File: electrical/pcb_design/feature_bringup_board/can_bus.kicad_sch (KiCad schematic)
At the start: 9 parts, among them J7 Molex_504050-0691, J8 Molex_504050-0691, U4 TCAN330DR

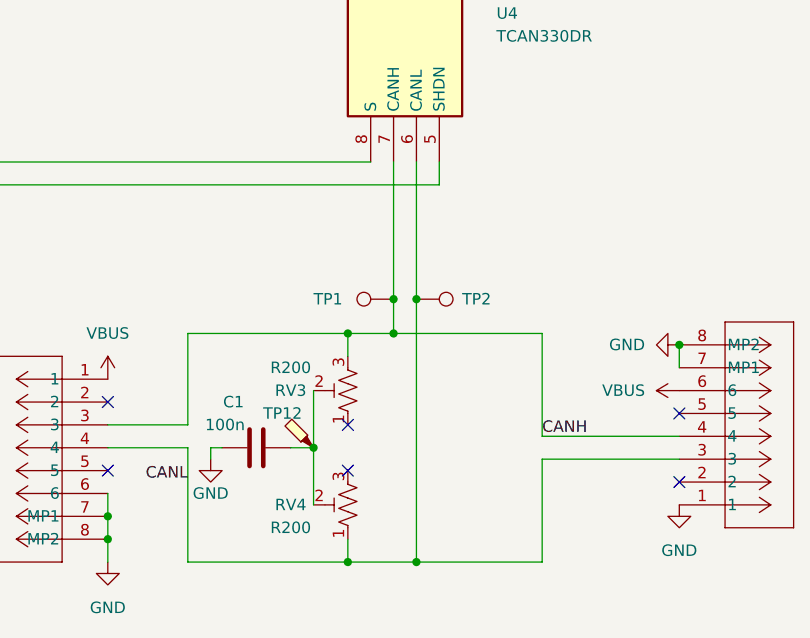
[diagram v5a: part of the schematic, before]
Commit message: Added 3rd button header. Also, fixed bugs introduced by cosmetic schematic changes.
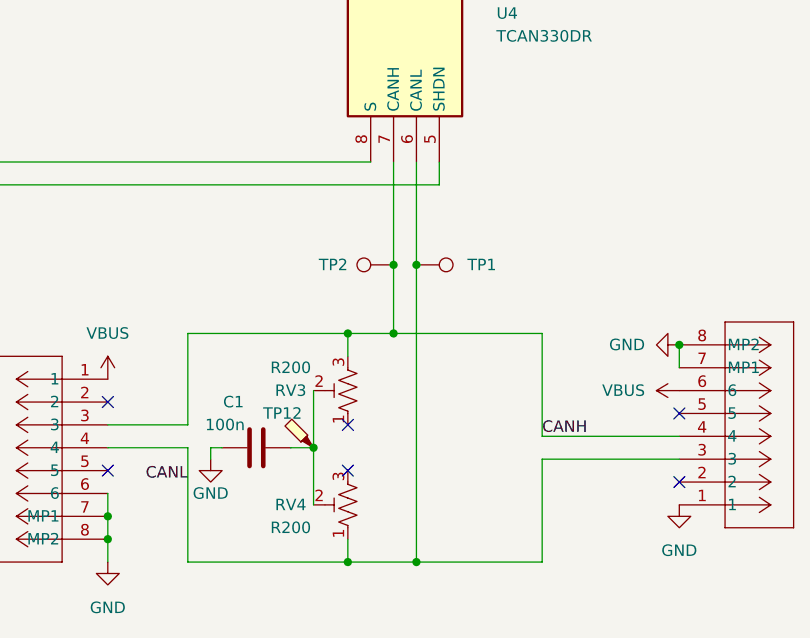
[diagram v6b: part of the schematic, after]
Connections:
- net CANH: now also TP2.1; no longer TP1.1
- net CANL: now also TP1.1; no longer TP2.1
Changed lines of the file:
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@@
   (junction (at 132.08 132.08) (diameter 0) (color 0 0 0 0)
   )
+  (junction (at 163.83 104.14) (diameter 0) (color 0 0 0 0)
+  )
   (junction (at 154.94 124.46) (diameter 0) (color 0 0 0 0)
   )
@@
   (junction (at 132.08 134.62) (diameter 0) (color 0 0 0 0)
   )
-  (junction (at 166.37 107.95) (diameter 0) (color 0 0 0 0)
-  )
-  (junction (at 163.83 107.95) (diameter 0) (color 0 0 0 0)
-  )
   (junction (at 166.37 137.16) (diameter 0) (color 0 0 0 0)
   )
   (junction (at 163.83 111.76) (diameter 0) (color 0 0 0 0)
+  )
+  (junction (at 166.37 104.14) (diameter 0) (color 0 0 0 0)
   )
   (no_connect (at 195.58 120.65))
@@
     (stroke (width 0) (type default))
   )
-  (wire (pts (xy 166.37 107.95) (xy 166.37 137.16))
+  (wire (pts (xy 166.37 92.71) (xy 166.37 104.14))
     (stroke (width 0) (type default))
   )
@@
     (stroke (width 0) (type default))
   )
-  (wire (pts (xy 166.37 92.71) (xy 166.37 107.95))
-    (stroke (width 0) (type default))
-  )
   (wire (pts (xy 180.34 123.19) (xy 180.34 111.76))
     (stroke (width 0) (type default))
@@
     (stroke (width 0) (type default))
   )
+  (wire (pts (xy 166.37 104.14) (xy 166.37 137.16))
+    (stroke (width 0) (type default))
+  )
   (wire (pts (xy 132.08 134.62) (xy 132.08 137.16))
     (stroke (width 0) (type default))
@@
     (stroke (width 0) (type default))
   )
+  (wire (pts (xy 163.83 104.14) (xy 163.83 111.76))
+    (stroke (width 0) (type default))
+  )
   (wire (pts (xy 158.75 137.16) (xy 166.37 137.16))
     (stroke (width 0) (type default))
@@
     (stroke (width 0) (type default))
   )
-  (wire (pts (xy 163.83 92.71) (xy 163.83 107.95))
-    (stroke (width 0) (type default))
-  )
-  (wire (pts (xy 163.83 107.95) (xy 163.83 111.76))
+  (wire (pts (xy 163.83 92.71) (xy 163.83 104.14))
     (stroke (width 0) (type default))
   )
@@
     )
   )
-  (symbol (lib_id "TVSC:TestPoint_Keystone_5002") (at 166.37 107.95 270) (unit 1)
-    (in_bom yes) (on_board yes) (dnp no)
-    (property "Reference" "TP2" (at 171.45 107.95 90)
-      (effects (font (size 1.27 1.27)) (justify left))
-    )
-    (property "Value" "TestPoint" (at 168.402 110.49 0)
-      (effects (font (size 1.27 1.27)) (justify left) hide)
-    )
-    (property "Footprint" "footprints:Keystone_5001" (at 166.37 113.03 0)
-      (effects (font (size 1.27 1.27)) hide)
-    )
-    (property "Datasheet" "https://www.keyelco.com/product.cfm/product_id/1310" (at 166.37 113.03 0)
-      (effects (font (size 1.27 1.27)) hide)
-    )
-    (property "Color" "White" (at 166.37 113.03 0)
-      (effects (font (size 1.27 1.27)) hide)
-    )
-    (property "Manufacturer" "Keystone" (at 166.37 107.95 0)
-      (effects (font (size 1.27 1.27)) hide)
-    )
-    (property "Manufacturer Part Number" "5001" (at 166.37 107.95 0)
-      (effects (font (size 1.27 1.27)) hide)
-    )
-    (property "MPN" "C238122" (at 166.37 107.95 0)
-      (effects (font (size 1.27 1.27)) hide)
-    )
-    (property "Active" "Y" (at 166.37 107.95 0)
-      (effects (font (size 1.27 1.27)) hide)
-    )
-    (pin "1")
-    (instances
-      (project "feature_bringup_board"
-        (path "/695f882b-5312-4493-b26d-8f7d6768a9db/d470ef27-6c0f-4ffa-83b6-2c4b3c9c5ff3"
-          (reference "TP2") (unit 1)
-        )
-      )
-    )
-  )
   (symbol (lib_id "power:VBUS") (at 132.08 116.84 0) (unit 1)
     (in_bom yes) (on_board yes) (dnp no) (fields_autoplaced)
@@
     )
   )
+  (symbol (lib_id "TVSC:TestPoint_Keystone_5002") (at 166.37 104.14 270) (unit 1)
+    (in_bom yes) (on_board yes) (dnp no)
+    (property "Reference" "TP1" (at 175.26 104.14 90)
+      (effects (font (size 1.27 1.27)) (justify right))
+    )
+    (property "Value" "TestPoint" (at 170.942 101.6 0)
+      (effects (font (size 1.27 1.27)) (justify right) hide)
+    )
+    (property "Footprint" "footprints:Keystone_5001" (at 166.37 109.22 0)
+      (effects (font (size 1.27 1.27)) hide)
+    )
+    (property "Datasheet" "https://www.keyelco.com/product.cfm/product_id/1310" (at 166.37 109.22 0)
+      (effects (font (size 1.27 1.27)) hide)
+    )
+    (property "Color" "White" (at 166.37 109.22 0)
+      (effects (font (size 1.27 1.27)) hide)
+    )
+    (property "Manufacturer" "Keystone" (at 166.37 104.14 0)
+      (effects (font (size 1.27 1.27)) hide)
+    )
+    (property "Manufacturer Part Number" "5001" (at 166.37 104.14 0)
+      (effects (font (size 1.27 1.27)) hide)
+    )
+    (property "MPN" "C238122" (at 166.37 104.14 0)
+      (effects (font (size 1.27 1.27)) hide)
+    )
+    (property "Active" "Y" (at 166.37 104.14 0)
+      (effects (font (size 1.27 1.27)) hide)
+    )
+    (pin "1")
+    (instances
+      (project "feature_bringup_board"
+        (path "/695f882b-5312-4493-b26d-8f7d6768a9db/d470ef27-6c0f-4ffa-83b6-2c4b3c9c5ff3"
+          (reference "TP1") (unit 1)
+        )
+      )
+    )
+  )
   (symbol (lib_id "power:GND") (at 143.51 125.73 0) (mirror y) (unit 1)
     (in_bom yes) (on_board yes) (dnp no)
@@
         (path "/695f882b-5312-4493-b26d-8f7d6768a9db/d470ef27-6c0f-4ffa-83b6-2c4b3c9c5ff3"
           (reference "TP12") (unit 1)
-        )
-      )
-    )
-  )
-  (symbol (lib_id "TVSC:TestPoint_Keystone_5002") (at 163.83 107.95 90) (unit 1)
-    (in_bom yes) (on_board yes) (dnp no)
-    (property "Reference" "TP1" (at 154.94 107.95 90)
-      (effects (font (size 1.27 1.27)) (justify right))
-    )
-    (property "Value" "TestPoint" (at 159.258 110.49 0)
-      (effects (font (size 1.27 1.27)) (justify right) hide)
-    )
-    (property "Footprint" "footprints:Keystone_5001" (at 163.83 102.87 0)
-      (effects (font (size 1.27 1.27)) hide)
-    )
-    (property "Datasheet" "https://www.keyelco.com/product.cfm/product_id/1310" (at 163.83 102.87 0)
-      (effects (font (size 1.27 1.27)) hide)
-    )
-    (property "Color" "White" (at 163.83 102.87 0)
-      (effects (font (size 1.27 1.27)) hide)
-    )
-    (property "Manufacturer" "Keystone" (at 163.83 107.95 0)
-      (effects (font (size 1.27 1.27)) hide)
-    )
-    (property "Manufacturer Part Number" "5001" (at 163.83 107.95 0)
-      (effects (font (size 1.27 1.27)) hide)
-    )
-    (property "MPN" "C238122" (at 163.83 107.95 0)
-      (effects (font (size 1.27 1.27)) hide)
-    )
-    (property "Active" "Y" (at 163.83 107.95 0)
-      (effects (font (size 1.27 1.27)) hide)
-    )
-    (pin "1")
-    (instances
-      (project "feature_bringup_board"
-        (path "/695f882b-5312-4493-b26d-8f7d6768a9db/d470ef27-6c0f-4ffa-83b6-2c4b3c9c5ff3"
-          (reference "TP1") (unit 1)
         )
       )
@@
         )
       )
+    )
+  )
+  (symbol (lib_id "TVSC:TestPoint_Keystone_5002") (at 163.83 104.14 90) (unit 1)
+    (in_bom yes) (on_board yes) (dnp no)
+    (property "Reference" "TP2" (at 158.75 104.14 90)
+      (effects (font (size 1.27 1.27)) (justify left))
+    )
+    (property "Value" "TestPoint" (at 161.798 101.6 0)
+      (effects (font (size 1.27 1.27)) (justify left) hide)
+    )
+    (property "Footprint" "footprints:Keystone_5001" (at 163.83 99.06 0)
+      (effects (font (size 1.27 1.27)) hide)
+    )
+    (property "Datasheet" "https://www.keyelco.com/product.cfm/product_id/1310" (at 163.83 99.06 0)
+      (effects (font (size 1.27 1.27)) hide)
+    )
+    (property "Color" "White" (at 163.83 99.06 0)
+      (effects (font (size 1.27 1.27)) hide)
+    )
+    (property "Manufacturer" "Keystone" (at 163.83 104.14 0)
+      (effects (font (size 1.27 1.27)) hide)
+    )
+    (property "Manufacturer Part Number" "5001" (at 163.83 104.14 0)
+      (effects (font (size 1.27 1.27)) hide)
+    )
+    (property "MPN" "C238122" (at 163.83 104.14 0)
+      (effects (font (size 1.27 1.27)) hide)
+    )
+    (property "Active" "Y" (at 163.83 104.14 0)
+      (effects (font (size 1.27 1.27)) hide)
+    )
+    (pin "1")
+    (instances
+      (project "feature_bringup_board"
+        (path "/695f882b-5312-4493-b26d-8f7d6768a9db/d470ef27-6c0f-4ffa-83b6-2c4b3c9c5ff3"
+          (reference "TP2") (unit 1)
+        )
+      )

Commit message: Added silkscreening to thank the Hacker Initiative
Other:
- company: (none) -> TVSC
- title: (none) -> Feature Bringup Board
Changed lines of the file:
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@@
 (kicad_sch (version 20230121) (generator eeschema)
-  (paper "A4")
+  (paper "USLetter")
+  (title_block
+    (title "Feature Bringup Board")
+    (date "2025-02-12")
+    (rev "${PCB_VERSION}")
+    (company "TVSC")
+  )
   (junction (at 158.75 137.16) (diameter 0) (color 0 0 0 0)
   )

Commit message: Fix several small issues on feature bringup board.
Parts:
- TP1, TP2: footprint footprints:Keystone_5001 -> footprints:Keystone_5002; MPN C238122 -> C238123; Manufacturer Part Number 5001 -> 5002
- U4: Arrow Part Number TCAN330DR -> (none); Arrow Price/Stock https://www.arrow.com/en/products/tcan330dr/texas-instrumen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 -> (none); Mouser Part Number 595-TCAN330DR -> (none); Mouser Price/Stock https://www.mouser.co.uk/ProductDetail/Texas-Instruments/TC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 -> (none)
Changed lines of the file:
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@@
-      (effects (font (size 1.27 1.27)) (justify left top) hide)
-    )
-    (property "Mouser Part Number" "595-TCAN330DR" (at 856.21 88.9 0)
-      (effects (font (size 1.27 1.27)) (justify left top) hide)
-    )
-    (property "Mouser Price/Stock" "https://www.mouser.co.uk/ProductDetail/Texas-Instruments/TCAN330DR?qs=9DwIlvx97afvSza3n7zoBw%3D%3D" (at 956.21 88.9 0)
-      (effects (font (size 1.27 1.27)) (justify left top) hide)
-    )
-    (property "Arrow Part Number" "TCAN330DR" (at 1056.21 88.9 0)
-      (effects (font (size 1.27 1.27)) (justify left top) hide)
-    )
-    (property "Arrow Price/Stock" "https://www.arrow.com/en/products/tcan330dr/texas-instruments?utm_currency=USD&region=europe" (at 1156.21 88.9 0)
       (effects (font (size 1.27 1.27)) (justify left top) hide)
     )
@@
       (effects (font (size 1.27 1.27)) (justify right) hide)
     )
-    (property "Footprint" "footprints:Keystone_5001" (at 166.37 109.22 0)
-      (effects (font (size 1.27 1.27)) hide)
-    )
-    (property "Datasheet" "https://www.keyelco.com/product.cfm/product_id/1310" (at 166.37 109.22 0)
+    (property "Footprint" "footprints:Keystone_5002" (at 166.37 109.22 0)
+      (effects (font (size 1.27 1.27)) hide)
+    )
+    (property "Datasheet" "https://www.keyelco.com/product.cfm/product_id/1311" (at 166.37 109.22 0)
       (effects (font (size 1.27 1.27)) hide)
     )
@@
       (effects (font (size 1.27 1.27)) hide)
     )
-    (property "Manufacturer Part Number" "5001" (at 166.37 104.14 0)
-      (effects (font (size 1.27 1.27)) hide)
-    )
-    (property "MPN" "C238122" (at 166.37 104.14 0)
+    (property "Manufacturer Part Number" "5002" (at 166.37 104.14 0)
+      (effects (font (size 1.27 1.27)) hide)
+    )
+    (property "MPN" "C238123" (at 166.37 104.14 0)
       (effects (font (size 1.27 1.27)) hide)
     )
@@
       (effects (font (size 1.27 1.27)) (justify left) hide)
     )
-    (property "Footprint" "footprints:Keystone_5001" (at 163.83 99.06 0)
-      (effects (font (size 1.27 1.27)) hide)
-    )
-    (property "Datasheet" "https://www.keyelco.com/product.cfm/product_id/1310" (at 163.83 99.06 0)
+    (property "Footprint" "footprints:Keystone_5002" (at 163.83 99.06 0)
+      (effects (font (size 1.27 1.27)) hide)
+    )
+    (property "Datasheet" "https://www.keyelco.com/product.cfm/product_id/1311" (at 163.83 99.06 0)
       (effects (font (size 1.27 1.27)) hide)
     )
@@
       (effects (font (size 1.27 1.27)) hide)
     )
-    (property "Manufacturer Part Number" "5001" (at 163.83 104.14 0)
-      (effects (font (size 1.27 1.27)) hide)
-    )
-    (property "MPN" "C238122" (at 163.83 104.14 0)
-      (effects (font (size 1.27 1.27)) hide)
-    )
+    (property "Manufacturer Part Number" "5002" (at 163.83 104.14 0)
+      (effects (font (size 1.27 1.27)) hide)
+    )
+    (property "MPN" "C238123" (at 163.83 104.14 0)
+      (effects (font (size 1.27 1.27)) hide)
+    )
